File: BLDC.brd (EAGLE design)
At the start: 75.9 x 52.1 mm, 120 parts, among them J1 1-770174-1, J2 1-770178-0, U1 MCP2562, U2 STM32F405RGT6, U3 DRV8302, U4 LM3671MF-3.3/NOPB, Y1 8MHz

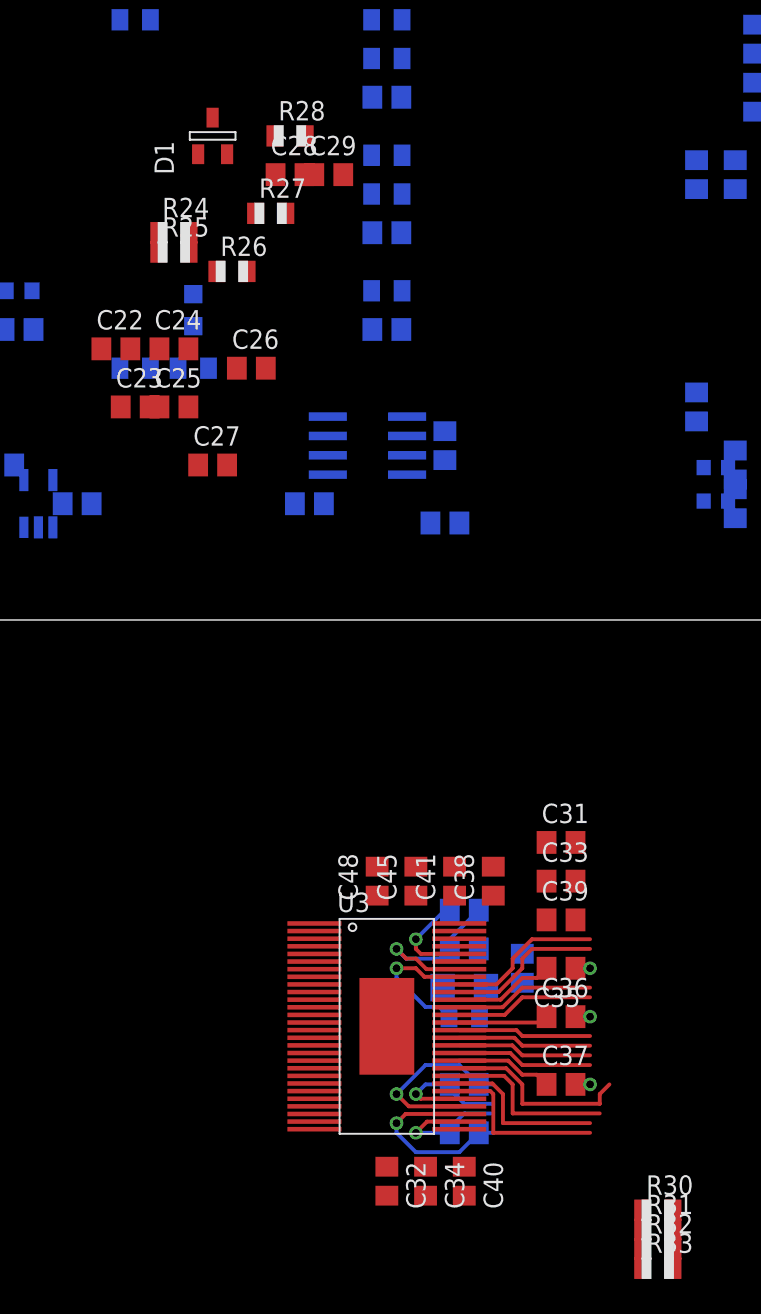
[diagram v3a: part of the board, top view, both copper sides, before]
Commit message: gate driver module progress
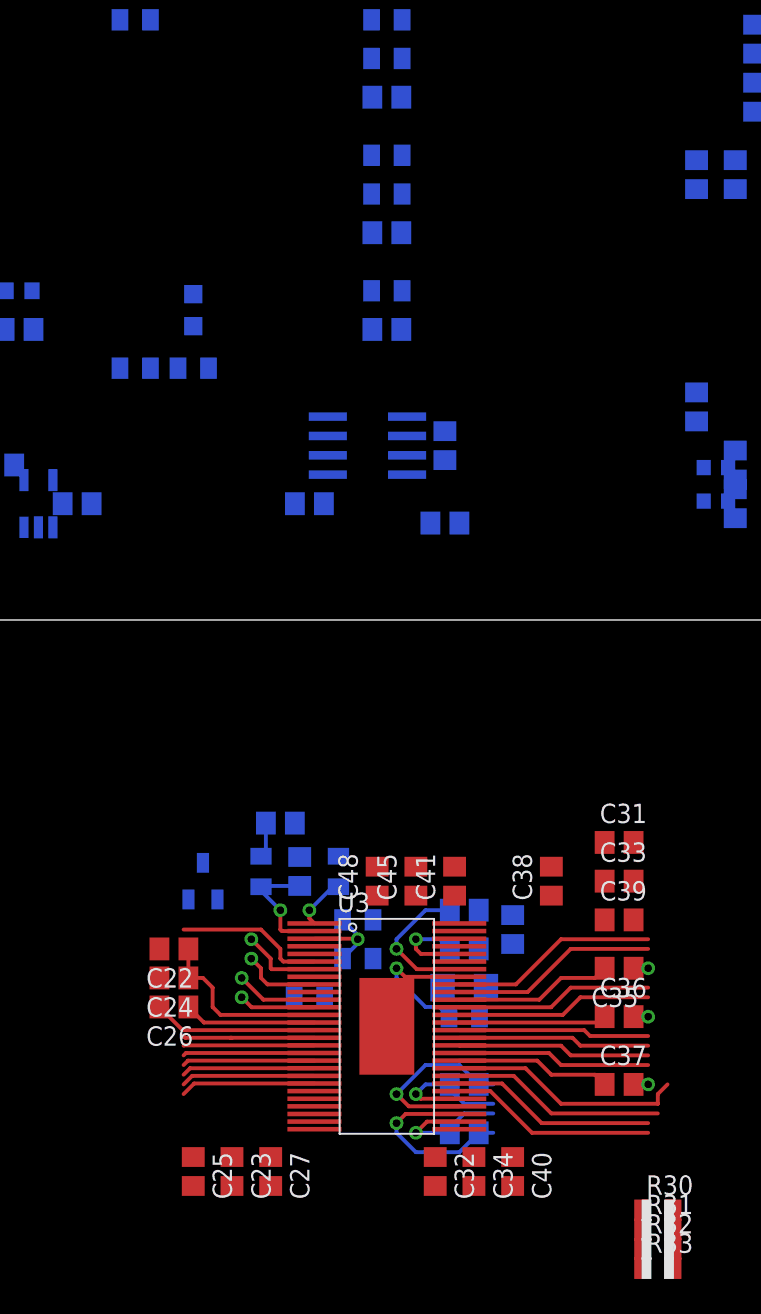
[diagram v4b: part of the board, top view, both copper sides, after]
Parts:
- moved C23 50.6 mm to (22.9, 15.9), turned to 270 degrees
- moved C25 50.2 mm to (20.3, 15.9), turned to 270 degrees
- moved D1 48.9 mm to (21.0, 34.9), flipped to the bottom
- moved R28 48.3 mm to (24.8, 35.6), flipped to the bottom, turned to 270 degrees
- moved R25 47.9 mm to (31.1, 29.8), flipped to the bottom, turned to 180 degrees
- moved R26 47.9 mm to (27.9, 27.3), flipped to the bottom
- moved R24 46.7 mm to (31.1, 32.4), flipped to the bottom
- moved C27 46.5 mm to (25.4, 15.9), turned to 270 degrees
- moved C29 45.8 mm to (27.3, 35.6), flipped to the bottom, turned to 90 degrees
- moved R27 43.4 mm to (29.8, 35.6), flipped to the bottom, turned to 90 degrees
- moved C28 42.5 mm to (26.0, 38.7), flipped to the bottom, turned to 180 degrees
- moved C26 42.2 mm to (19.1, 26.7), turned to 180 degrees
- moved C24 41.3 mm to (19.1, 28.6), turned to 180 degrees
- moved C22 39.6 mm to (19.1, 30.5), turned to 180 degrees
- moved C31 3.81 mm to (48.3, 37.5)
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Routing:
- net N$16: track 0.00 -> 12.2 mm
- net N$19: track 0.00 -> 10.8 mm
- net FAULT: track 0.00 -> 9.83 mm
- net L3: track 0.00 -> 8.87 mm
- net H3: track 0.00 -> 8.82 mm
- net L2: track 0.00 -> 8.76 mm
- net EN_GATE: track 0.00 -> 8.75 mm
- net H2: track 0.00 -> 8.71 mm
- net N$17: track 0.00 -> 8.69 mm
- net L1: track 0.00 -> 8.65 mm
- net H1: track 0.00 -> 8.59 mm
- net N$12: track 0.00 -> 8.17 mm, vias 0 -> 1
- net N$13: track 0.00 -> 6.23 mm, vias 0 -> 1
- net N$14: track 0.00 -> 5.60 mm, vias 0 -> 1
- net N$15: track 0.00 -> 5.37 mm, vias 0 -> 1
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
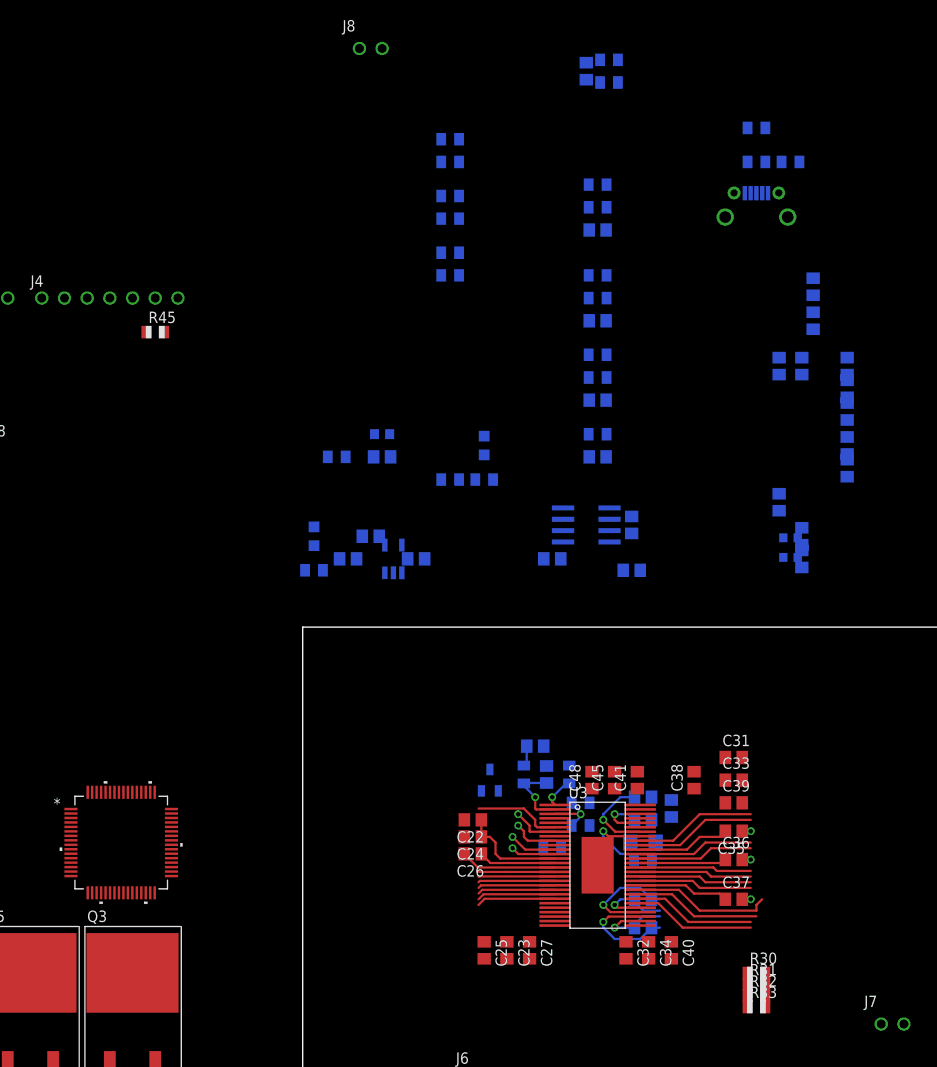
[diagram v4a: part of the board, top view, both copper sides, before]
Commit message: consdensed gate driver module
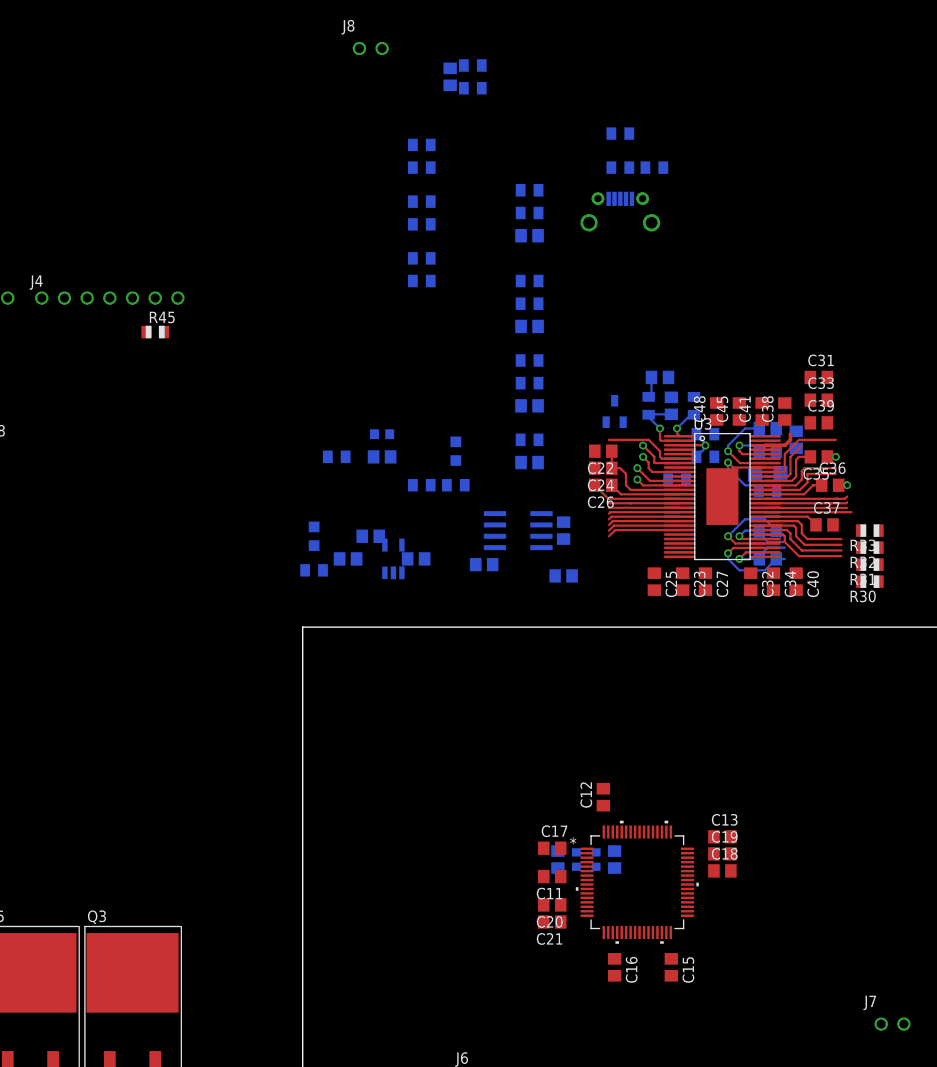
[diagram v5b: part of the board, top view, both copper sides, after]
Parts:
- moved C21 76.9 mm to (27.9, 19.1), flipped to the top, turned to 180 degrees
- moved C20 71.6 mm to (27.9, 21.0), flipped to the top, turned to 180 degrees
- moved C16 69.8 mm to (34.9, 14.0), flipped to the top, turned to 270 degrees
- moved C15 65.3 mm to (41.3, 14.0), flipped to the top, turned to 270 degrees
- moved C17 63.3 mm to (27.9, 27.3), flipped to the top, turned to 0 degrees
- moved U2 58.0 mm to (37.5, 23.5)
- moved C18 57.2 mm to (47.0, 24.8), flipped to the top, turned to 0 degrees
- moved C19 55.0 mm to (47.0, 26.7), flipped to the top, turned to 0 degrees
- moved R33 54.8 mm to (63.5, 62.9), turned to 180 degrees
- moved R32 51.7 mm to (63.5, 61.0), turned to 180 degrees
- moved C11 49.0 mm to (27.9, 24.1), flipped to the top, turned to 180 degrees
- moved R31 48.7 mm to (63.5, 59.1), turned to 180 degrees
- moved C13 46.0 mm to (47.0, 28.6), flipped to the top, turned to 0 degrees
- moved C12 45.8 mm to (33.7, 33.0), flipped to the top
- moved C23 45.7 mm to (42.5, 57.1)
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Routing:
- net M_H1: track 13.6 -> 6.69 mm
- net M_H3: track 15.5 -> 9.98 mm
- net H3_VS: track 15.0 -> 10.0 mm, vias 1 -> 0
- net VCC: track 0.00 -> 4.25 mm
- net N$27: track 10.2 -> 6.11 mm
- net M_L1: track 12.9 -> 9.31 mm
- net H1_LOW: track 12.9 -> 9.25 mm
- net H3_LOW: track 13.5 -> 9.96 mm
- net M_L3: track 13.5 -> 9.90 mm
- net M_L2: track 12.7 -> 9.23 mm
- net H2_VS: track 13.6 -> 10.3 mm
- net N$23: track 14.6 -> 11.5 mm
- net GND: track 12.7 -> 9.70 mm
- net M_H2: track 12.6 -> 9.57 mm
- net N$25: track 9.70 -> 6.79 mm
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
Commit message: stm32 module progress
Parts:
- moved C12 16.3 mm to (27.9, 17.8), turned to 180 degrees
- moved C17 16.3 mm to (33.7, 12.1), turned to 90 degrees
- moved C21 15.6 mm to (41.9, 12.1), turned to 270 degrees
- moved C20 15.0 mm to (40.0, 12.1), turned to 270 degrees
- moved C11 15.0 mm to (36.8, 12.1), turned to 270 degrees
- moved C13 14.8 mm to (32.4, 31.1), turned to 90 degrees
- moved C10 14.8 mm to (34.9, 12.7), turned to 0 degrees
- moved C19 13.5 mm to (34.3, 31.1), turned to 90 degrees
- moved C16 13.1 mm to (47.0, 19.1), turned to 0 degrees
- moved C15 12.8 mm to (47.0, 25.4), turned to 0 degrees
- moved C18 12.5 mm to (36.2, 31.1), turned to 90 degrees
- moved Y1 10.6 mm to (34.9, 15.9), turned to 270 degrees
- moved C9 6.98 mm to (34.9, 19.1), turned to 180 degrees
- moved U2 1.91 mm to (37.5, 21.6), turned to 90 degrees
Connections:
- net HALL_1_IN: no longer R10.1, R11.1, R6.1, R7.1
- net HALL_1_OUT: no longer C4.1, C5.1, R10.2, R11.2
- net HALL_2_IN: now also R10.1, R11.1, R6.1, R7.1
- net HALL_2_OUT: now also C4.1, R10.2
- net HALL_3_OUT: now also C5.1, R11.2

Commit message: stm32 module progress
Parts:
- moved R19 81.3 mm to (27.9, 23.5), flipped to the top, turned to 90 degrees
- moved R18 80.1 mm to (27.9, 27.3), flipped to the top, turned to 270 degrees
- moved R21 74.7 mm to (26.0, 23.5), flipped to the top, turned to 90 degrees
- moved R20 73.5 mm to (26.0, 27.3), flipped to the top, turned to 270 degrees
- moved R23 68.2 mm to (24.1, 23.5), flipped to the top, turned to 90 degrees
- moved R22 66.9 mm to (24.1, 27.3), flipped to the top, turned to 270 degrees
- moved C13 26.8 mm to (42.5, 6.35), turned to 270 degrees
- moved C18 26.1 mm to (44.5, 6.35), turned to 270 degrees
- moved C19 25.6 mm to (40.6, 6.35), turned to 270 degrees
- moved C15 23.3 mm to (27.9, 12.1), turned to 180 degrees
- moved C16 19.1 mm to (27.9, 18.4), turned to 180 degrees
- moved C12 17.8 mm to (45.7, 18.4), turned to 270 degrees
- moved C17 17.7 mm to (44.5, 26.0), turned to 270 degrees
- moved C10 15.1 mm to (43.2, 25.4), turned to 180 degrees
- moved C21 14.8 mm to (35.6, 25.4), turned to 90 degrees
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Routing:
- net N$36: track 0.00 -> 34.9 mm
- net SENS3: track 0.00 -> 10.4 mm
- net SENS2: track 0.00 -> 5.84 mm
- net TX_SDA_NSS: track 0.00 -> 3.24 mm
- net RX_SCL_MOSI: track 0.00 -> 3.19 mm
- net HALL_3_OUT: track 0.00 -> 2.82 mm, vias 0 -> 1
- net EN_GATE: track 8.11 -> 10.8 mm, vias 0 -> 1
- net N$8: track 0.00 -> 2.59 mm, vias 0 -> 1
- net CAR_CAN_RX: track 0.00 -> 2.56 mm, vias 0 -> 1
- net SENS1: track 0.00 -> 2.52 mm
- net FAULT: track 9.19 -> 11.4 mm, vias 0 -> 1
- net HALL_2_OUT: track 0.00 -> 2.13 mm, vias 0 -> 1
- net TEMP_MOTOR: track 0.00 -> 1.92 mm, vias 0 -> 1
- net HALL_1_OUT: track 0.00 -> 1.82 mm, vias 0 -> 1
- net AN_IN: track 0.00 -> 1.71 mm, vias 0 -> 1
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
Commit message: stm32 module progress
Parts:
- moved R18 45.1 mm to (73.0, 29.5)
- moved R19 45.1 mm to (73.0, 25.7)
- moved R20 45.1 mm to (71.1, 29.5)
- moved R21 45.1 mm to (71.1, 25.7)
- moved R22 45.1 mm to (69.2, 29.5)
- moved R23 45.1 mm to (69.2, 25.7)
- moved D1 37.9 mm to (42.2, 39.1), turned to 270 degrees
- moved C22 36.4 mm to (46.7, 37.8), turned to 270 degrees
- moved C28 35.9 mm to (38.4, 44.1), turned to 90 degrees
- moved C24 35.4 mm to (48.6, 37.8), turned to 270 degrees
- moved C26 34.5 mm to (50.5, 37.8), turned to 270 degrees
- moved R28 34.1 mm to (41.6, 42.9), turned to 180 degrees
- moved C29 31.4 mm to (41.6, 45.4), turned to 0 degrees
- moved R27 29.0 mm to (41.6, 47.9), turned to 0 degrees
- moved C31 26.5 mm to (38.4, 61.9), turned to 90 degrees
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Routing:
- net SENS2: track 5.84 -> 39.8 mm
- net SENS1: track 2.52 -> 35.6 mm
- net L3: track 9.77 -> 1.53 mm
- net SENS3: track 10.4 -> 17.6 mm
- net FAULT: track 11.4 -> 5.56 mm, vias 1 -> 2
- net +3V3: track 5.21 -> 10.0 mm
- net EN_GATE: track 10.8 -> 7.95 mm, vias 1 -> 2
- net H3: track 9.78 -> 7.24 mm, vias 1 -> 2
- net N$14: track 5.60 -> 3.16 mm
- net L2: track 9.67 -> 7.26 mm, vias 1 -> 2
- net H1: track 9.47 -> 7.13 mm, vias 1 -> 2
- net H2: track 9.62 -> 7.34 mm, vias 1 -> 2
- net L1: track 9.52 -> 7.38 mm, vias 1 -> 2
- net ADC_TEMP: track 1.21 -> 2.83 mm
